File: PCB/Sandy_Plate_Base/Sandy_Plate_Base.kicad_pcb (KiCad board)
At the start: 2 copper layers, 285 x 84.3 mm, 1 part

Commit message: 更新：ビルドナンバー　→　DN0030
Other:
- board text added: "#Sandy_kbd DN0030, Plate for Base by @jpskenn"
- board text removed: "#Sandy_kbd DN0020, Plate for Base by @jpskenn"

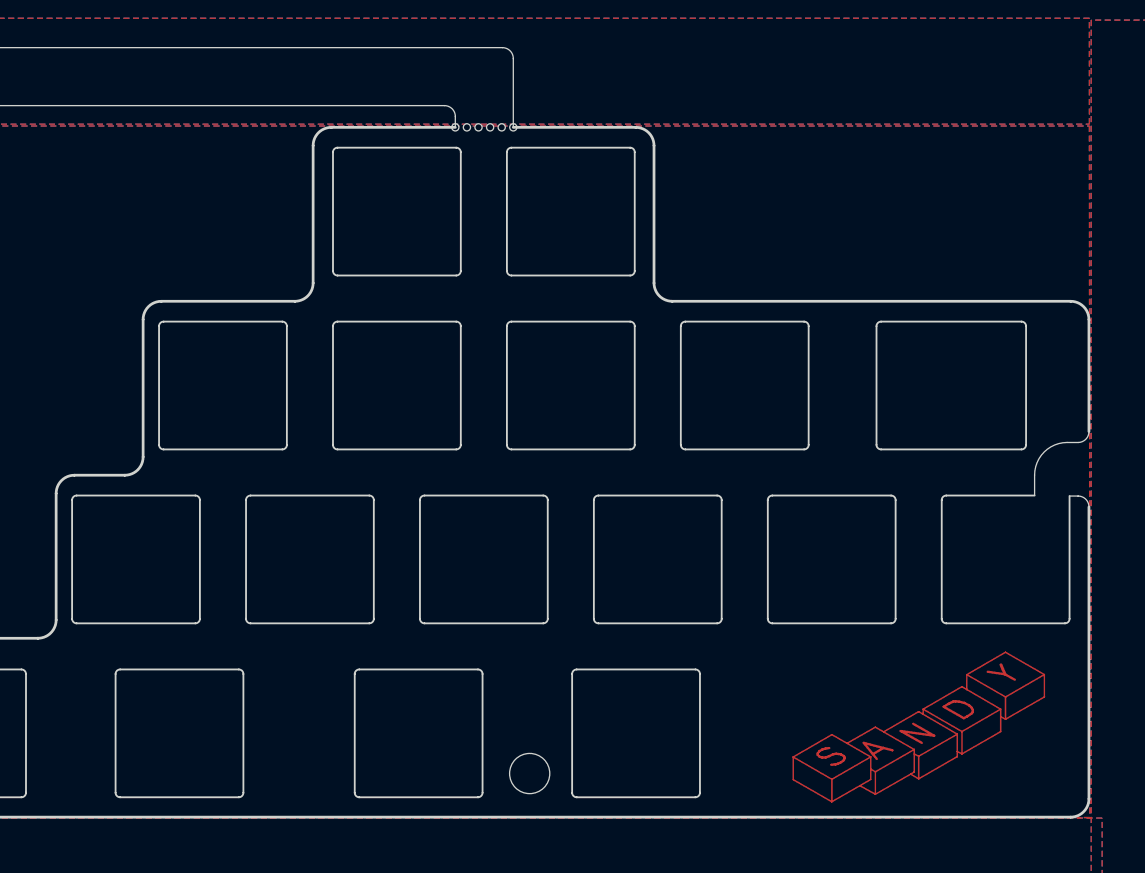
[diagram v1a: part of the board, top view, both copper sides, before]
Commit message: 修正：右インジケータLEDを廃止したのに、プレートにディフューザーが残っていた
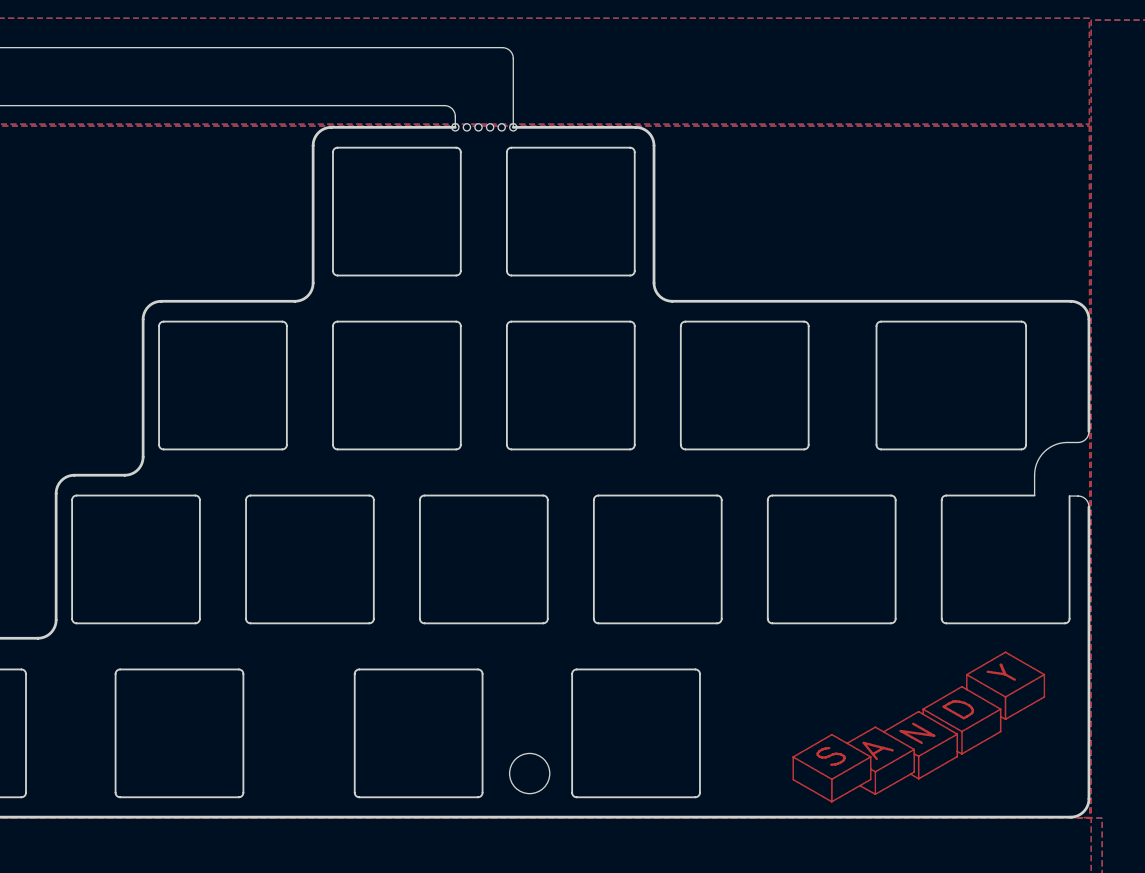
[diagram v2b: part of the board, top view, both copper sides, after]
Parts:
- REF**: footprint locallib:60_Outline-Sandy-Plate-Base6 -> locallib:60_Outline-Sandy-Plate-Base7

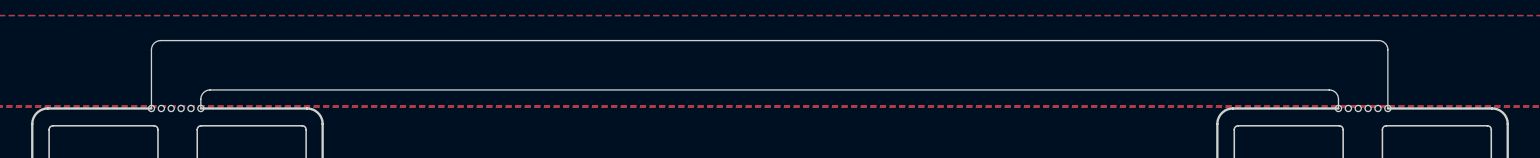
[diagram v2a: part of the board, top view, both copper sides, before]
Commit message: 3Dモデルチェック用に捨て基板なしのBase用プレートを作成
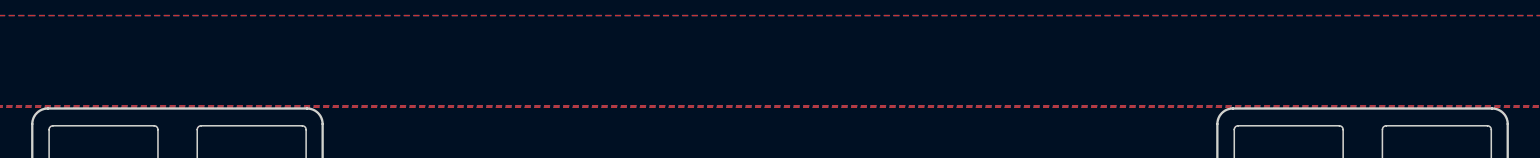
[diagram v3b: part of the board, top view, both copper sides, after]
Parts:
- REF**: footprint locallib:60_Outline-Sandy-Plate-Base7 -> locallib:60_Outline-Sandy-Plate-Base7-wo-frame
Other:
- board size 285 x 84.3 mm -> 285 x 75.6 mm
